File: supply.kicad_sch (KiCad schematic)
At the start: 1 part, among them J6 Molex_Nano-Fit_1x2_SMD_105430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

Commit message: [#100765] Update subsheets
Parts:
- removed J6: Molex_Nano-Fit_1x2_SMD_1054301202, antmicro-footprints:Conn_Molex_Nano-Fit_1x2_SMD_1054301202, symbol antmicroWire2BoardConnectors:Molex_Nano-Fit_1x2_SMD_1054301202
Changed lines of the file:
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@@
 	(generator_version "10.0")
 	(paper "A4")
+	(hierarchical_label "POWER_EN"
+		(shape input)
+		(at 52.07 66.04 180)
+		(effects
+			(font
+				(size 1.27 1.27)
+			)
+			(justify right)
+		)
+	)
 	(symbol
-		(lib_id "antmicroWire2BoardConnectors:Molex_Nano-Fit_1x2_SMD_1054301202")
-		(at 43.18 72.39 0)
+		(lib_id "antmicropower:+3V3")
+		(at 170.18 27.94 0)
 		(unit 1)
 		(body_style 1)
@@
 		(dnp no)
 		(fields_autoplaced yes)
-		(property "Reference" "J6"
-			(at 50.8 73.66 0)
-			(show_name no)
-			(do_not_autoplace no)
-			(effects
-				(font
-					(size 1.27 1.27)
-					(thickness 0.15)
-				)
-				(justify left)
-			)
-		)
-		(property "Value" "Molex_Nano-Fit_1x2_SMD_1054301202"
-			(at 69.85 80.01 0)
-			(hide yes)
-			(show_name no)
-			(do_not_autoplace no)
-			(effects
-				(font
-					(size 1.27 1.27)
-					(thickness 0.15)
-				)
-				(justify left bottom)
-			)
-		)
-		(property "Footprint" "antmicro-footprints:Conn_Molex_Nano-Fit_1x2_SMD_1054301202"
-			(at 69.85 82.55 0)
-			(hide yes)
-			(show_name no)
-			(do_not_autoplace no)
-			(effects
-				(font
-					(size 1.27 1.27)
-					(thickness 0.15)
-				)
-				(justify left bottom)
-			)
-		)
-		(property "Datasheet" "https://www.farnell.com/cad/3578051.pdf"
-			(at 69.85 85.09 0)
-			(hide yes)
-			(show_name no)
-			(do_not_autoplace no)
-			(effects
-				(font
-					(size 1.27 1.27)
-					(thickness 0.15)
-				)
-				(justify left bottom)
-			)
-		)
-		(property "Description" "Pin Header, Pitch 2.5 mm, 1 Row, 2 Contacts, Nano-Fit"
-			(at 69.85 95.25 0)
-			(hide yes)
-			(show_name no)
-			(do_not_autoplace no)
-			(effects
-				(font
-					(size 1.27 1.27)
-				)
-				(justify left bottom)
-			)
-		)
-		(property "Manufacturer" "Molex"
-			(at 69.85 87.63 0)
-			(hide yes)
-			(show_name no)
-			(do_not_autoplace no)
-			(effects
-				(font
-					(size 1.27 1.27)
-					(thickness 0.15)
-				)
-				(justify left bottom)
-			)
-		)
-		(property "MPN" "105430-1202"
-			(at 50.8 76.2 0)
-			(show_name no)
-			(do_not_autoplace no)
-			(effects
-				(font
-					(size 1.27 1.27)
-					(thickness 0.15)
-				)
-				(justify left)
+		(property "Reference" "#PWR05"
+			(at 185.42 27.94 0)
+			(hide yes)
+			(show_name no)
+			(do_not_autoplace no)
+			(effects
+				(font
+					(size 1.27 1.27)
+					(thickness 0.15)
+				)
+				(justify left bottom)
+			)
+		)
+		(property "Value" "+3V3"
+			(at 170.18 22.86 0)
+			(show_name no)
+			(do_not_autoplace no)
+			(effects
+				(font
+					(size 1.27 1.27)
+					(thickness 0.15)
+				)
+			)
+		)
+		(property "Footprint" ""
+			(at 185.42 35.56 0)
+			(hide yes)
+			(show_name no)
+			(do_not_autoplace no)
+			(effects
+				(font
+					(size 1.27 1.27)
+					(thickness 0.15)
+				)
+				(justify left bottom)
+			)
+		)
+		(property "Datasheet" ""
+			(at 185.42 38.1 0)
+			(hide yes)
+			(show_name no)
+			(do_not_autoplace no)
+			(effects
+				(font
+					(size 1.27 1.27)
+					(thickness 0.15)
+				)
+				(justify left bottom)
+			)
+		)
+		(property "Description" ""
+			(at 185.42 40.64 0)
+			(hide yes)
+			(show_name no)
+			(do_not_autoplace no)
+			(effects
+				(font
+					(size 1.27 1.27)
+				)
+				(justify left bottom)
 			)
 		)
 		(property "Author" "Antmicro"
-			(at 69.85 90.17 0)
+			(at 185.42 30.48 0)
 			(hide yes)
 			(show_name no)
@@
 		)
 		(property "License" "Apache-2.0"
-			(at 69.85 92.71 0)
-			(hide yes)
-			(show_name no)
-			(do_not_autoplace no)
-			(effects
-				(font
-					(size 1.27 1.27)
-					(thickness 0.15)
-				)
-				(justify left bottom)
-			)
-		)
-		(pin "MP"
-		)
-		(pin "2"
+			(at 185.42 33.02 0)
+			(hide yes)
+			(show_name no)
+			(do_not_autoplace no)
+			(effects
+				(font
+					(size 1.27 1.27)
+					(thickness 0.15)
+				)
+				(justify left bottom)
+			)
 		)
 		(pin "1"
@@
 			(project "antmicro-jetson-orin-baseboard-pcie-switch-expansion-hw"
 				(path "/9f8272ef-d62d-4578-9094-a2852fcd4bf4/b2048f45-d77d-4bd2-929a-db82e576fe70"
-					(reference "J6")
+					(reference "#PWR05")
 					(unit 1)
 				)
+			)
+		)
+	)
+	(symbol
+		(lib_id "antmicropower:+1V8")
+		(at 176.53 27.94 0)
+		(unit 1)
+		(body_style 1)
+		(exclude_from_sim no)
+		(in_bom yes)
+		(on_board yes)
+		(in_pos_files yes)
+		(dnp no)
+		(fields_autoplaced yes)
+		(property "Reference" "#PWR06"
+			(at 191.77 30.48 0)
+			(hide yes)
+			(show_name no)
+			(do_not_autoplace no)
+			(effects
+				(font
+					(size 1.27 1.27)
+					(thickness 0.15)
+				)
+				(justify left bottom)
+			)
+		)
+		(property "Value" "+1V8"
+			(at 176.53 22.86 0)
+			(show_name no)
+			(do_not_autoplace no)
+			(effects
+				(font
+					(size 1.27 1.27)
+					(thickness 0.15)
+				)
+			)
+		)
+		(property "Footprint" ""
+			(at 191.77 35.56 0)
+			(hide yes)
+			(show_name no)
+			(do_not_autoplace no)
+			(effects
+				(font
+					(size 1.27 1.27)
+					(thickness 0.15)
+				)
+				(justify left bottom)
+			)
+		)
+		(property "Datasheet" ""
+			(at 191.77 38.1 0)
+			(hide yes)
+			(show_name no)
+			(do_not_autoplace no)
+			(effects
+				(font
+					(size 1.27 1.27)
+					(thickness 0.15)
+				)
+				(justify left bottom)
+			)
+		)
+		(property "Description" ""
+			(at 191.77 40.64 0)
+			(hide yes)
+			(show_name no)
+			(do_not_autoplace no)
+			(effects
+				(font
+					(size 1.27 1.27)
+				)
+				(justify left bottom)
+			)
+		)
+		(property "Author" "Antmicro"
+			(at 191.77 33.02 0)
+			(hide yes)
+			(show_name no)
+			(do_not_autoplace no)
+			(effects
+				(font
+					(size 1.27 1.27)
+					(thickness 0.15)
+				)
+				(justify left bottom)
+			)
+		)
+		(property "License" "Apache-2.0"
+			(at 191.77 35.56 0)
+			(hide yes)
+			(show_name no)
+			(do_not_autoplace no)
+			(effects
+				(font
+					(size 1.27 1.27)
+					(thickness 0.15)
+				)
+				(justify left bottom)
+			)
+		)
+		(pin "1"
+		)
+		(instances
+			(project "antmicro-jetson-orin-baseboard-pcie-switch-expansion-hw"
+				(path "/9f8272ef-d62d-4578-9094-a2852fcd4bf4/b2048f45-d77d-4bd2-929a-db82e576fe70"
+					(reference "#PWR06")
+					(unit 1)
+				)
+			)
+		)
+	)
+	(symbol
+		(lib_id "antmicropower:+0V95")
+		(at 182.88 27.94 0)
+		(unit 1)
+		(body_style 1)
+		(exclude_from_sim no)
+		(in_bom yes)
+		(on_board yes)
+		(in_pos_files yes)
+		(dnp no)
+		(fields_autoplaced yes)
+		(property "Reference" "#PWR07"
+			(at 182.88 31.75 0)
+			(hide yes)
+			(show_name no)
+			(do_not_autoplace no)
+			(effects
+				(font
+					(size 1.27 1.27)
+				)
+			)
+		)
+		(property "Value" "+0V95"
+			(at 182.88 22.86 0)
+			(show_name no)
+			(do_not_autoplace no)
+			(effects
+				(font
+					(size 1.27 1.27)
+				)
+			)
+		)
+		(property "Footprint" ""
+			(at 182.88 27.94 0)
+			(hide yes)
+			(show_name no)
+			(do_not_autoplace no)
+			(effects
+				(font
+					(size 1.27 1.27)
+				)
+			)
+		)
+		(property "Datasheet" ""
+			(at 182.88 27.94 0)
+			(hide yes)
+			(show_name no)
+			(do_not_autoplace no)
+			(effects
+				(font
+					(size 1.27 1.27)
+				)
+			)
+		)
+		(property "Description" ""
+			(at 182.88 34.29 0)
+			(hide yes)
+			(show_name no)
+			(do_not_autoplace no)
+			(effects
+				(font
+					(size 1.27 1.27)
+				)
+				(justify left bottom)
+			)
+		)
+		(pin "1"
+		)
+		(instances
+			(project "antmicro-jetson-orin-baseboard-pcie-switch-expansion-hw"
+				(path "/9f8272ef-d62d-4578-9094-a2852fcd4bf4/b2048f45-d77d-4bd2-929a-db82e576fe70"
+					(reference "#PWR07")
+					(unit 1)
+				)

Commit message: [#100765] Update schematic
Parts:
- added C121, C125: C_100n_0402, jetson-orin-baseboard-footprints:C_0402_1005Metric, symbol jetson-orin-baseboard:C_100n_0402
- added C122, C151: C_22u_25V_0805, jetson-orin-baseboard-footprints:C_0805_2012Metric, symbol jetson-orin-baseboard:C_22u_25V_0805
- added C123: C_1u_0402, jetson-orin-baseboard-footprints:C_0402_1005Metric, symbol jetson-orin-baseboard:C_1u_0402
- added C126, C127, C128, C154: C_22u_16V_0603, jetson-orin-baseboard-footprints:C_0603_1608Metric_EIA, symbol jetson-orin-baseboard:C_22u_16V_0603
- added C155: C_4u7_25V_0402, jetson-orin-baseboard-footprints:C_0402_1005Metric, symbol jetson-orin-baseboard:C_4u7_25V_0402
- added C306, C314, C317: C_22u_25V_0805, antmicro-footprints:C_0805_2012Metric, symbol antmicroCapacitorsmisc:C_22u_25V_0805
- added C309: C_100n_0402, antmicro-footprints:C_0402_1005Metric, symbol antmicroCapacitors0402:C_100n_0402
- added C81, C82, C88, C89, C90, C91: C_10u_0402, antmicro-footprints:C_0402_1005Metric, symbol antmicroCapacitors0402:C_10u_0402
- added C83: C_1u_0402, antmicro-footprints:C_0402_1005Metric, symbol antmicroCapacitors0402:C_1u_0402
- added C87: C_120p_100V_0402, antmicro-footprints:C_0402_1005Metric, symbol antmicroCapacitors0402:C_120p_100V_0402
- added D17: LED_G_0603_LG_L29K-G2J1-24-Z, antmicro-footprints:LED_0603_1608Metric_G, symbol antmicroLEDIndicationDiscrete:LED_G_0603_LG_L29K-G2J1-24-Z
- added D306: LED_G_0603_KP-1608CGCK, antmicro-footprints:LED_0603_1608Metric_G, symbol antmicroLEDIndicationDiscrete:LED_G_0603_KP-1608CGCK
- added D33: ESD9X5.0ST5G, jetson-orin-baseboard-footprints:SOD-923, symbol jetson-orin-baseboard:ESD9X5.0ST5G
- added L1: L_560n_17.7A_Bourns-SRP5030CA, jetson-orin-baseboard-footprints:L_Bourns-SRP5030CA, symbol jetson-orin-baseboard:L_560n_17.7A_Bourns-SRP5030CA
- added L2: L_220n_5.9A_1008, antmicro-footprints:L_1008_2520Metric, symbol antmicroFixedInductors:L_220n_5.9A_1008
- added L3: L_2u2_5.8A_WE-PMFI-35329222, antmicro-footprints:L_WE-PMFI-353220, symbol antmicroFixedInductors:L_2u2_5.8A_WE-PMFI-35329222
- added Q1: BSS138PW,115, antmicro-footprints:SC70-3, symbol antmicroTransistorsFETsMOSFETsSingle:BSS138PW,115
- added R147: R_100k_0.1%_0402, antmicro-footprints:R_0402_1005Metric, symbol antmicroResistors0402:R_100k_0.1%_0402
- added R148, R22: R_0R_0402, antmicro-footprints:R_0402_1005Metric, symbol antmicroResistors0402:R_0R_0402
- added R15: R_1k5_0402, antmicro-footprints:R_0402_1005Metric, symbol antmicroResistors0402:R_1k5_0402
- added R16: R_470R_0402, antmicro-footprints:R_0402_1005Metric, symbol antmicroResistors0402:R_470R_0402
- added R17: R_59k_0402, antmicro-footprints:R_0402_1005Metric, symbol antmicroResistors0402:R_59k_0402
- added R173, R176, R240: R_499k_0402, jetson-orin-baseboard-footprints:R_0402_1005Metric, symbol jetson-orin-baseboard:R_499k_0402
- added R178: R_0R_22.4A_0603, jetson-orin-baseboard-footprints:R_0603_1608Metric, symbol jetson-orin-baseboard:R_0R_22.4A_0603
- added R18: R_12k4_0402, antmicro-footprints:R_0402_1005Metric, symbol antmicroResistors0402:R_12k4_0402
- added R19: R_13k7_0402, antmicro-footprints:R_0402_1005Metric, symbol antmicroResistors0402:R_13k7_0402
- added R20: R_47k_0402, antmicro-footprints:R_0402_1005Metric, symbol antmicroResistors0402:R_47k_0402
- added R21: R_330R_0402, antmicro-footprints:R_0402_1005Metric, symbol antmicroResistors0402:R_330R_0402
- added R23: R_45k3_0402, antmicro-footprints:R_0402_1005Metric, symbol antmicroResistors0402:R_45k3_0402
- added R24, R312, R66: R_10k_0402, antmicro-footprints:R_0402_1005Metric, symbol antmicroResistors0402:R_10k_0402
- added R323: R_0R_22.4A_0603, antmicro-footprints:R_0603_1608Metric, symbol antmicroResistors0603:R_0R_22.4A_0603
- added R71: R_33R_0402, antmicro-footprints:R_0402_1005Metric, symbol antmicroResistors0402:R_33R_0402
- added TP15: TP_1mm_SMD, antmicro-footprints:TP_SMD_1mm, symbol antmicroTestPoints:TP_1mm_SMD
- added TP309: TP_0.75mm_SMD, antmicro-footprints:TP_SMD_0.75mm, symbol antmicroTestPoints:TP_0.75mm_SMD
- added TP54: TP_0.75mm_SMD, jetson-orin-baseboard-footprints:TP_SMD_0.75mm, symbol jetson-orin-baseboard:TP_0.75mm_SMD
- added U21: TPS62A06DRLR, antmicro-footprints:SOT-563, symbol antmicroDCDCConverters:TPS62A06DRLR
- added U302: AP62301_TSOT, antmicro-footprints:TSOT23-6, symbol antmicroDCDCConverters:AP62301_TSOT
- added U40: SIC431AED-T1-GE3, jetson-orin-baseboard-footprints:MLP44-24L_4x4x0.75mm, symbol jetson-orin-baseboard:SIC431AED-T1-GE3
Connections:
- net +0V95: now also R148.2, TP15.1
- net +1V8: now also R21.2, R323.2, TP309.1
- net +3V3: now also C81.2, C82.2, D33.1 (C), R15.1, R16.2, R178.2, R66.2, TP54.1, U21.3 (VIN)
- net POWER_EN: now also R22.1
- new net: C87.2, C88.2, C89.2, C90.2, C91.2, L2.2, R148.1, R17.2
- new net: C87.1, R147.2, R17.1, U21.5 (FB)
- new net: D17.2 (A), R16.1
- new net: D306.2 (A), R21.1
- new net: U40.10 (GL), U40.11 (GL), U40.28 (GL)
- new net: Q1.1 (G), R66.1, R71.1
- new net: R71.2, U21.6 (PG)
- new net: C309.2, U302.6 (BST)
- new net: D17.1 (C), Q1.3 (D)
- new net: L2.1, U21.2 (SW)
- new net 3V3_BOOT: C125.2, U40.23 (BOOT)
- new net 3V3_EN: R22.2, U40.19 (EN)
- new net 3V3_FB: R23.1, R24.2, U40.17 (FB)
- new net 3V3_MODE1: R176.2, R240.1, U40.21 (MODE1)
- new net 3V3_MODE2: R173.2, U40.20 (MODE2)
- new net 3V3_OUT: C126.2, C127.2, C128.2, C154.2, L1.2, R178.1, R23.2, U40.18 (V_{OUT})
- new net 3V3_PHASE: C125.1, U40.24 (PHASE)
- new net 3V3_SW: L1.1, U40.5 (SW), U40.6 (SW), U40.7 (SW), U40.8 (SW), U40.9 (SW)
- new net 3V3_VDD: C123.2, R240.2, U40.15 (V_{DD})
- new net 3V3_VDRV: C155.2, U40.12 (V_{DRV})
- new net DCDC_EN: C83.1, R15.2, U21.4 (EN)
- new net EN_3V3: R20.1, R312.2, U302.5 (EN)
- new net FB_3V3: R18.1, R19.2, U302.4 (FB)
- new net GND: C121.2, C122.1, C123.1, C126.1, C127.1, C128.1, C151.1, C154.1, C155.1, C306.2, C314.2, C317.2, C81.1, C82.1, C83.2, C88.1, C89.1, C90.1, C91.1, D306.1 (C), D33.2 (A), Q1.2 (S), R147.1, R173.1, R176.1, R19.1, R24.1, R312.1, U21.1 (GND), U302.1 (GND), U40.13 (P_{GND}), U40.16 (A_{GND}), U40.25 (A_{GND}), U40.27 (P_{GND}), U40.3 (P_{GND}), U40.4 (P_{GND})
- new net OUT_3V3: C314.1, C317.1, L3.2, R18.2, R323.1
- new net SW_3V3: C309.1, L3.1, U302.2 (SW)
- new net VCC: C121.1, C122.2, C151.2, C306.1, R20.2, U302.3 (VIN), U40.1 (V_{IN}), U40.2 (V_{IN}), U40.22 (V_{IN}), U40.26 (V_{IN})
- no-connect marks 0 -> 2
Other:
- note added: "3V3 DCDC"
- note added: "R_{FB_H} = (R_{FB_L}(V_{OUT}-0.6))/0.6"
- note added: "TODO: what signal should enable the converter?"
- note added: "V_{OUT} = 0,954V"
- note added: "V_{OUT} = 0.6*(45k3+10k)/10k = 3.318[V]"
- note added: "V_{OUT} = 0.6*(59k/100k + 1)"
- note added: "V_{OUT} = 0.6*(R_{FB_H}+R_{FB_L})/R_{FB_L}"
- note added: "V_{OUT} = 0.6*(R_{FB_H}/R_{FB_L} + 1)"

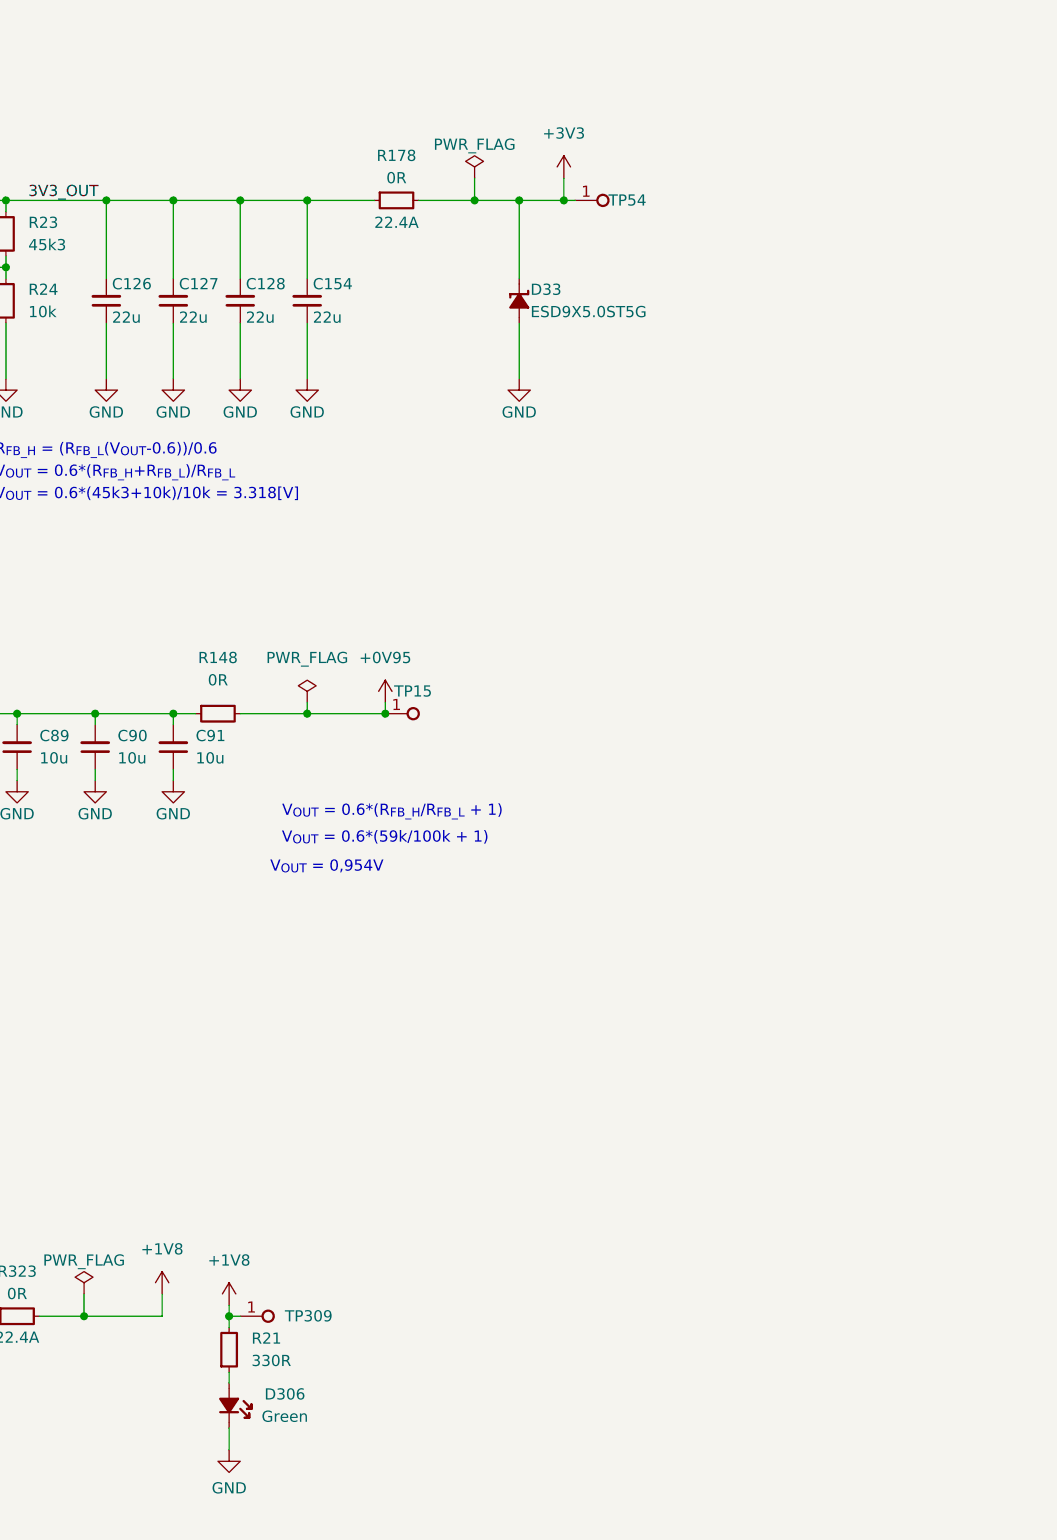
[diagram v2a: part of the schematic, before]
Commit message: [#100765] Add Control LEDs, update Power section
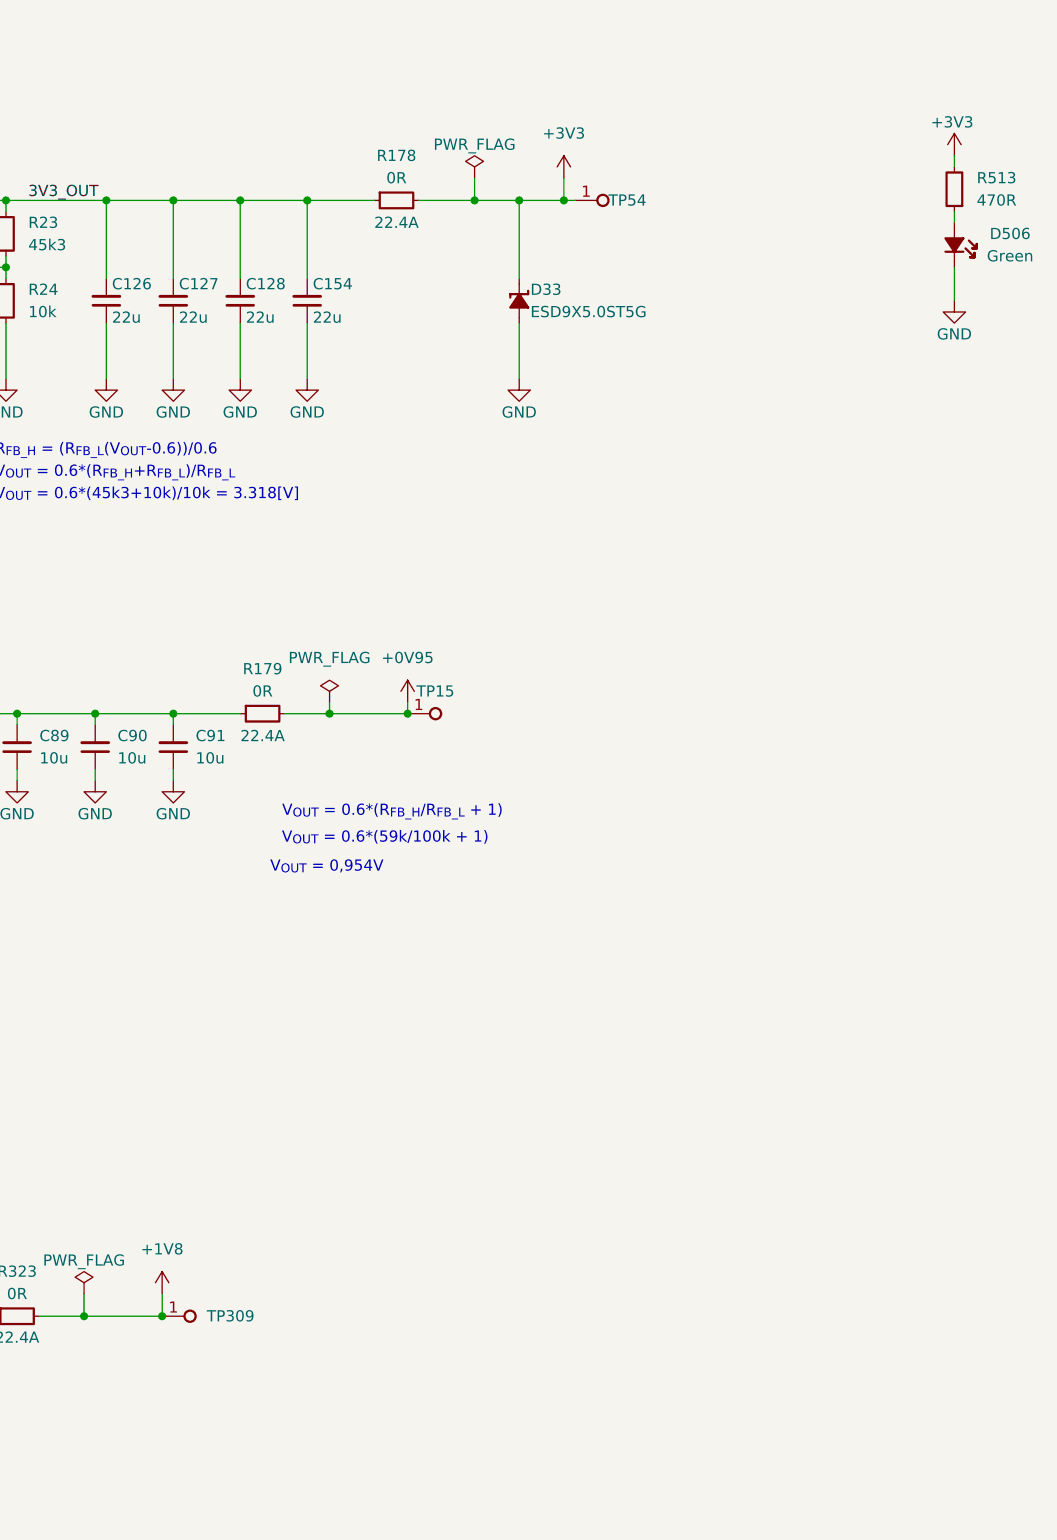
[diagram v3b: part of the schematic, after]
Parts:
- removed D306: LED_G_0603_KP-1608CGCK, antmicro-footprints:LED_0603_1608Metric_G, symbol antmicroLEDIndicationDiscrete:LED_G_0603_KP-1608CGCK
- removed R148: R_0R_0402, antmicro-footprints:R_0402_1005Metric, symbol antmicroResistors0402:R_0R_0402
- removed R21: R_330R_0402, antmicro-footprints:R_0402_1005Metric, symbol antmicroResistors0402:R_330R_0402
- added D506: LED_G_0603_KP-1608CGCK, antmicro-footprints:LED_0603_1608Metric_G, symbol antmicroLEDIndicationDiscrete:LED_G_0603_KP-1608CGCK
- added R179: R_0R_22.4A_0603, jetson-orin-baseboard-footprints:R_0603_1608Metric, symbol jetson-orin-baseboard:R_0R_22.4A_0603
- added R513: R_470R_0402, antmicro-footprints:R_0402_1005Metric, symbol antmicroResistors0402:R_470R_0402
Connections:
- net +0V95: now also R179.2
- net +3V3: now also R513.2
- net GND: now also D506.1 (C)
- net at C87.2, C88.2, C89.2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: now also R179.1
- new net: D506.2 (A), R513.1
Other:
- moved on the sheet: TP15, TP309
